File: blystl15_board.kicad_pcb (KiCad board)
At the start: 2 copper layers, 3 parts, among them P2 ARM JTAG/SWD

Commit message: Schematic Draft
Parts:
- removed BT1: BAT-HLD-003-SMT, 1_I-SYST_inc:BAT_BAT-HLD-003-SMT
- removed P2: ARM JTAG/SWD, 1_I-SYST_inc:CON10_2X5_DUK_FTSH_SAI-M
- added C1: 4.7 μF, Capacitor_SMD:C_0603_1608Metric, F.Cu at (151.9, 106.8)
- added C2: 10000 pF, Capacitor_SMD:C_0402_1005Metric, F.Cu at (162.9, 90.6)
- added C3: 10µF, Capacitor_SMD:C_0603_1608Metric, F.Cu at (151.9, 109.3)
- added C4: 10000 pF, Capacitor_SMD:C_0402_1005Metric, F.Cu at (162.9, 92.6)
- added C5: 10000 pF, Capacitor_SMD:C_0402_1005Metric, F.Cu at (162.9, 94.6)
- added C6: 10000 pF, Capacitor_SMD:C_0402_1005Metric, F.Cu at (162.9, 96.6)
- added L1: 1.0µH, Inductor_SMD:L_0805_2012Metric, F.Cu at (156.2, 106.9)
- added R1: 4.7k, Resistor_SMD:R_0402_1005Metric, F.Cu at (155.4, 109.3)
- added R2: 4.7K, Resistor_SMD:R_0402_1005Metric, F.Cu at (155.4, 111.3)
- added SW2: SW_Push, Button_Switch_SMD:SW_Push_1P1T_NO_CK_KSC7xxJ, F.Cu at (144.8, 93.5)
- added SW3: SW_Push, Button_Switch_SMD:SW_Push_1P1T_NO_CK_KSC7xxJ, F.Cu at (144.8, 101.3)
- added SW4: SW_Push, Button_Switch_SMD:SW_Push_1P1T_NO_CK_KSC7xxJ, F.Cu at (144.8, 109.0)
- added U1: NPM1304-QEAA-R7, 1_I-SYST_inc:QFN50P500X500X90-33N, F.Cu at (153.9, 101.9)
- added U2: MAX30102EFD+T, 1_I-SYST_inc:21-1048_F143A5&plus_1_MXM-L, F.Cu at (160.6, 101.8)
- added U3: MAX30208CLB+T, 1_I-SYST_inc:21-100265_MXM, F.Cu at (160.4, 107.4)
- moved M1 14.8 mm to (156.7, 94.0)

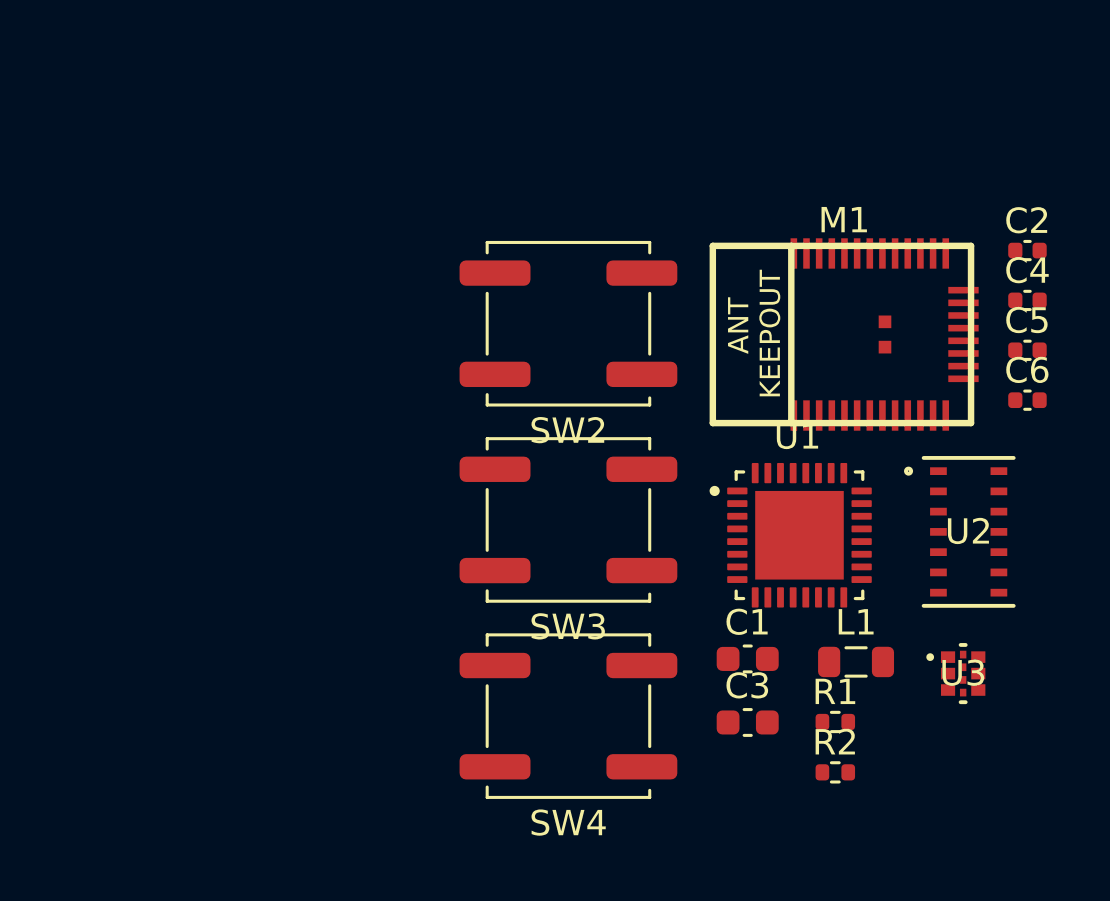
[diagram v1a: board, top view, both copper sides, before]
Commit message: All footprints imported in PCB editor
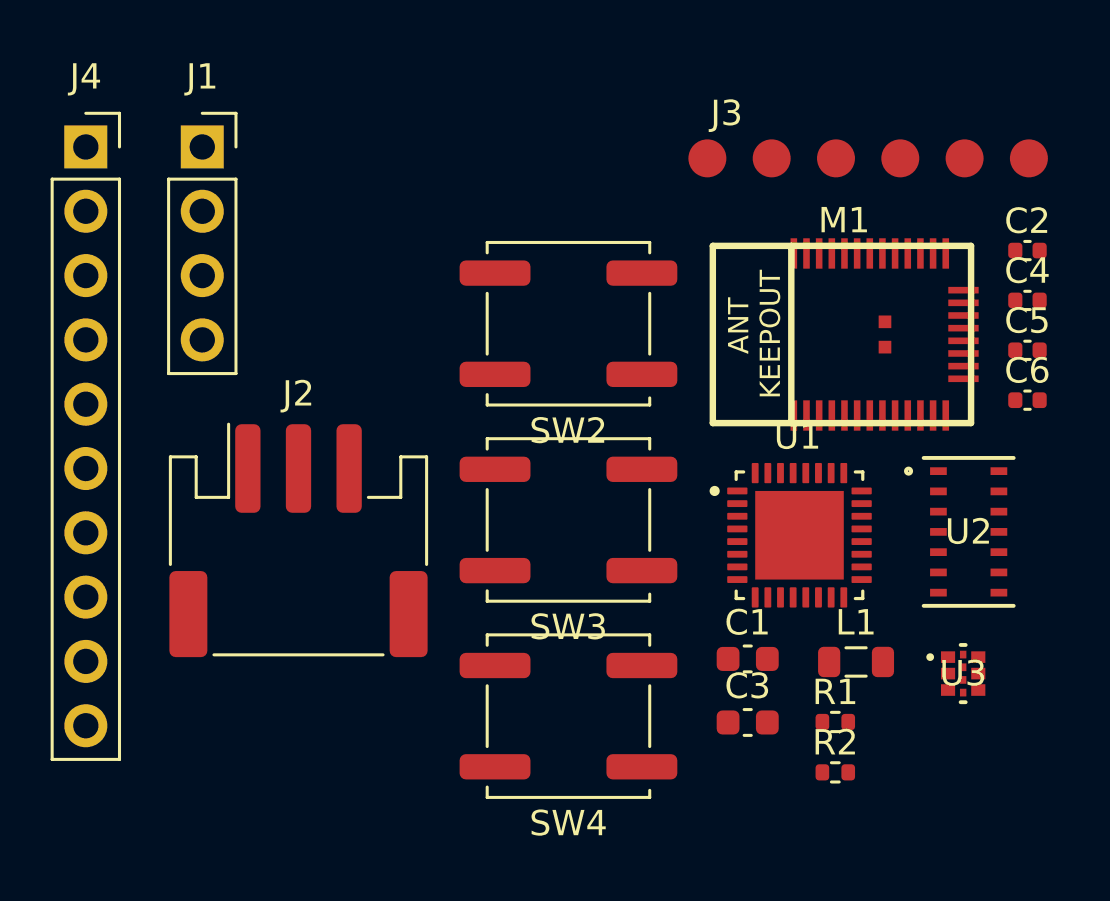
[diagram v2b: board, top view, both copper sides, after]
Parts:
- added J1: SSD1306, Connector_PinSocket_2.54mm:PinSocket_1x04_P2.54mm_Vertical, F.Cu at (130.3, 86.5)
- added J2: Conn_01x03, Connector_JST:JST_PH_S3B-PH-SM4-TB_1x03-1MP_P2.00mm_Horizontal, F.Cu at (134.2, 102.1)
- added J3: DOCK_PADS, 1_I-SYST_inc:Dock_Pads_6Pin, F.Cu at (156.7, 87.0)
- added J4: BNO085, Connector_PinSocket_2.54mm:PinSocket_1x10_P2.54mm_Vertical, F.Cu at (125.8, 86.5)

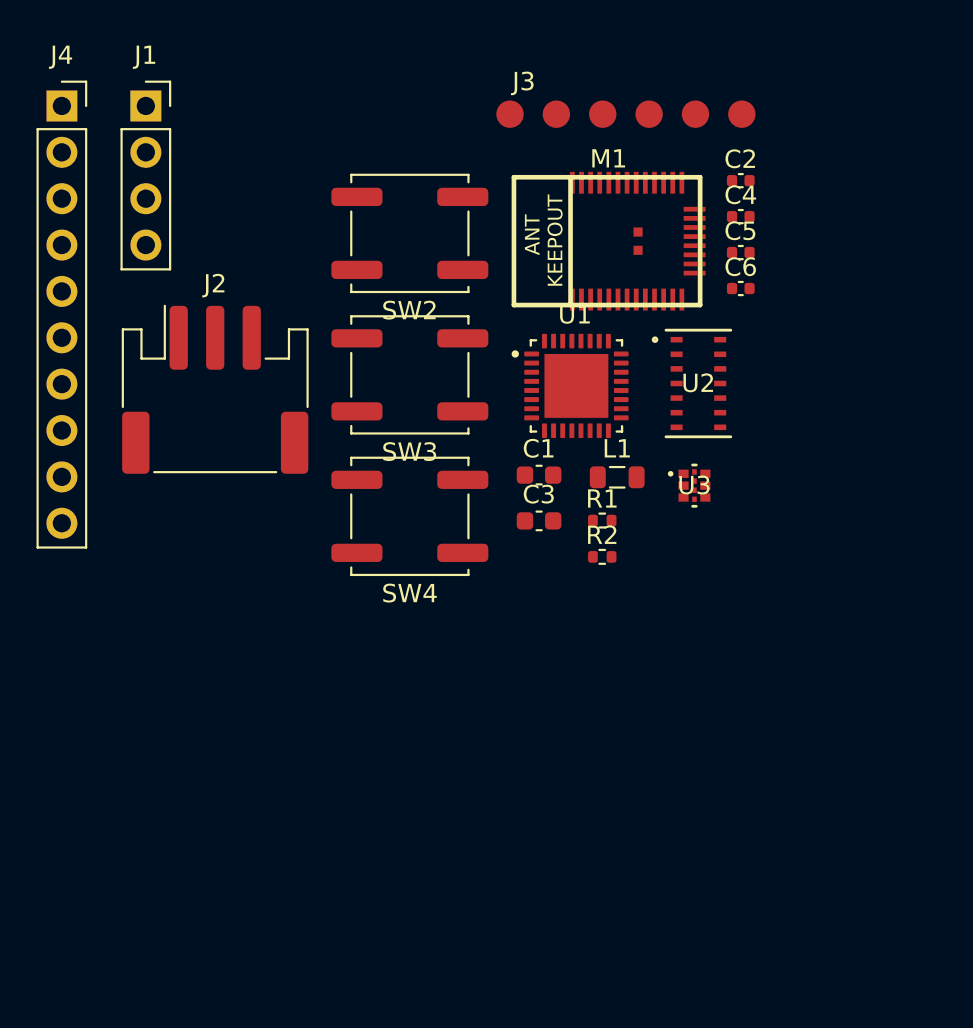
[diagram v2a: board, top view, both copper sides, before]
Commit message: Created custom footprints to match dimension of external boards
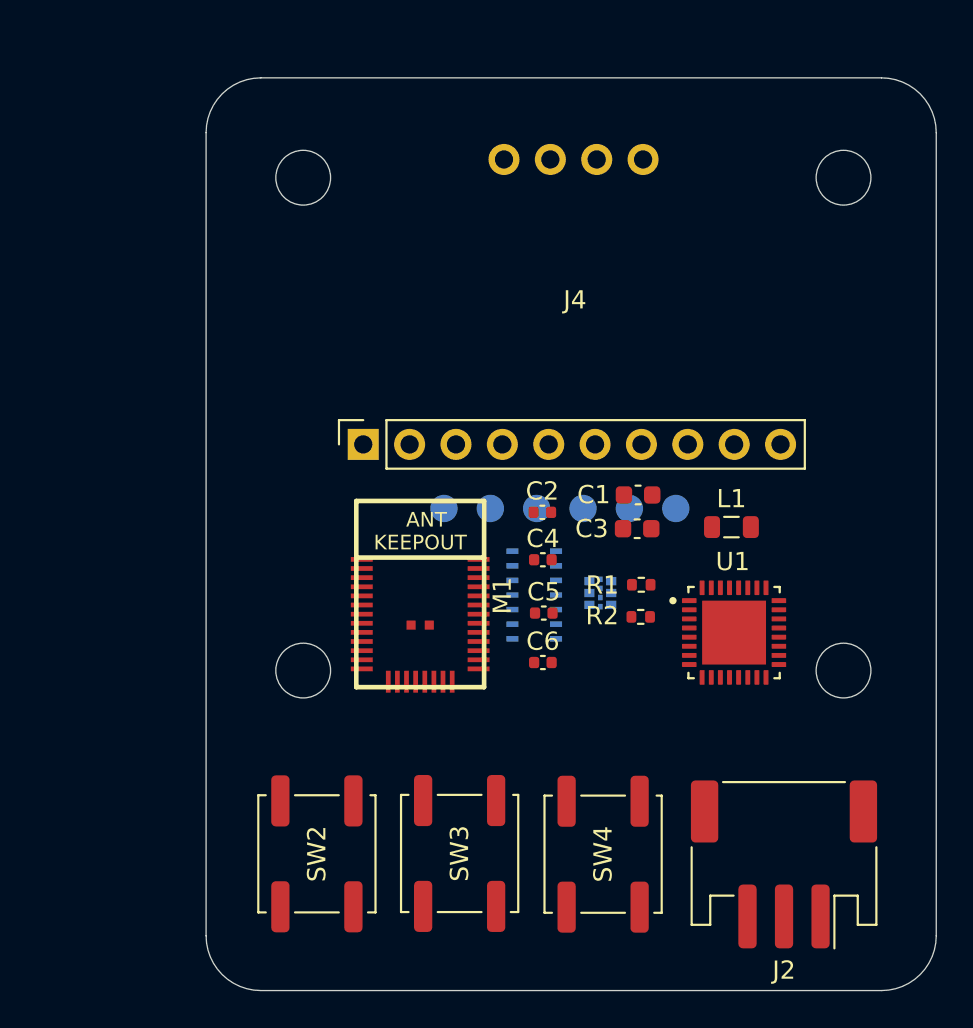
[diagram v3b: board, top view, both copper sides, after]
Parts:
- J1: footprint Connector_PinSocket_2.54mm:PinSocket_1x04_P2.54mm_Vertical -> 1_I-SYST_inc:OLED_1.3in_I2C
- J3, U2, U3: moved to B.Cu
- J4: footprint Connector_PinSocket_2.54mm:PinSocket_1x10_P2.54mm_Vertical -> 1_I-SYST_inc:BNO085_Module
- moved J2 40.6 mm to (165.3, 128.1), turned to 180 degrees
- moved SW2 34.4 mm to (139.7, 127.5), turned to 90 degrees
- moved J4 30.5 mm to (153.8, 98.5), turned to 90 degrees
- moved J1 29.2 mm to (153.8, 104.0)
- moved SW3 26.4 mm to (147.5, 127.5), turned to 90 degrees
- moved M1 23.4 mm to (145.4, 114.4), turned to -90 degrees
- moved C6 23.2 mm to (152.1, 117.0)
- moved C5 22.5 mm to (152.2, 114.3)
- moved J3 21.9 mm to (153.0, 108.6), turned to 180 degrees
- moved C4 21.7 mm to (152.1, 111.4)
- moved SW4 21.3 mm to (155.4, 127.5), turned to 90 degrees
- moved C2 21.2 mm to (152.1, 108.8)
- moved U1 16.0 mm to (162.6, 115.4)
- moved U2 14.7 mm to (151.6, 113.3), turned to 180 degrees
- moved U3 7.82 mm to (155.2, 113.2), turned to 180 degrees
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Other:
- board outline added: 40 x 50 mm

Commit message: Organized components in pcb layout editor
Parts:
- removed C2: 10000 pF, Capacitor_SMD:C_0402_1005Metric
- removed J2: Conn_01x03, Connector_JST:JST_PH_S3B-PH-SM4-TB_1x03-1MP_P2.00mm_Horizontal
- removed J3: DOCK_PADS, 1_I-SYST_inc:Dock_Pads_6Pin
- removed J4: BNO085, 1_I-SYST_inc:BNO085_Module
- removed R1: 4.7k, Resistor_SMD:R_0402_1005Metric
- removed R2: 4.7K, Resistor_SMD:R_0402_1005Metric
- added C10: 10µF, Capacitor_SMD:C_0603_1608Metric, F.Cu at (152.5, 97.0)
- added C11: 0.1µF, Capacitor_SMD:C_0603_1608Metric, F.Cu at (146.5, 99.5)
- added C12: 0.1 μF, Capacitor_SMD:C_0402_1005Metric, F.Cu at (159.0, 104.5)
- added C13: 1µF, Capacitor_SMD:C_0603_1608Metric, F.Cu at (152.0, 93.3)
- added C14: 0.1 μF, Capacitor_SMD:C_0402_1005Metric, F.Cu at (161.0, 116.0)
- added C7: 0.1 μF, Capacitor_SMD:C_0402_1005Metric, F.Cu at (159.0, 99.0)
- added C8: 0.1 μF, Capacitor_SMD:C_0402_1005Metric, F.Cu at (157.0, 95.5)
- added C9: 0.01 μF, Capacitor_SMD:C_0402_1005Metric, F.Cu at (135.0, 107.5)
- added J5: Conn_01x03, Connector_JST:JST_PH_S3B-PH-SM4-TB_1x03-1MP_P2.00mm_Horizontal, F.Cu at (147.5, 115.7)
- added J6: DOCK_PADS, 1_I_Syst.inc:Dock_Pads_6Pin, B.Cu at (152.5, 100.8)
- added R3: 10kΩ, Resistor_SMD:R_0402_1005Metric, F.Cu at (160.5, 92.5)
- added R4: 4.7kΩ, Resistor_SMD:R_0402_1005Metric, F.Cu at (163.5, 97.0)
- added R5: 4.7kΩ, Resistor_SMD:R_0402_1005Metric, F.Cu at (163.5, 93.5)
- added R6: 10kΩ, Resistor_SMD:R_0402_1005Metric, F.Cu at (158.0, 115.5)
- added U6: W25Q80DVSSIG, 1_I_Syst.inc:WIN_SS-8_WIN-L, F.Cu at (160.1, 109.6)
- added U7: OPT3001DNPRQ1, 1_I_Syst.inc:SON65P200X200X65-7N, F.Cu at (161.0, 119.0)
- added U8: LSM6DSV80X, 1_I_Syst.inc:QFN_LSM6DSV80XTR_STM-M, F.Cu at (160.0, 95.8)
- C4, C5, C6: value 10000 pF -> 0.01 μF
- J1: footprint 1_I-SYST_inc:OLED_1.3in_I2C -> 1_I_Syst.inc:OLED_1.3in_I2C
- M1: value ~ -> BLYSTL15; footprint 1_I-SYST_inc:BLYSTL15 -> 1_I_Syst.inc:BLYSTL15
- SW2, SW3, SW4: footprint Button_Switch_SMD:SW_Push_1P1T_NO_CK_KSC7xxJ -> Button_Switch_SMD:SW_Push_1P1T-MP_NO_Horizontal_Alps_SKRTLAE010
- U1: value NPM1304-QEAA-R7 -> NPM1304; footprint 1_I-SYST_inc:QFN50P500X500X90-33N -> 1_I_Syst.inc:QFN50P500X500X90-33N
- U2: footprint 1_I-SYST_inc:21-1048_F143A5&plus_1_MXM-L -> 1_I_Syst.inc:21-1048_F143A5&plus_1_MXM-L
- U3: footprint 1_I-SYST_inc:21-100265_MXM -> 1_I_Syst.inc:21-100265_MXM
- moved SW2 39.8 mm to (169.5, 101.2)
- moved SW3 39.5 mm to (169.5, 94.7)
- moved C6 26.7 mm to (166.5, 94.5), turned to 90 degrees
- moved L1 25.3 mm to (143.0, 93.4), turned to -90 degrees
- moved U1 25.0 mm to (147.8, 95.2)
- moved SW4 24.2 mm to (169.4, 107.9)
- moved C3 21.8 mm to (146.0, 91.0)
- moved C4 17.8 mm to (166.5, 101.0), turned to 90 degrees
- moved C1 17.0 mm to (143.0, 98.8), turned to 90 degrees
- moved M1 15.5 mm to (137.0, 101.3), turned to 0 degrees
- moved C5 15.0 mm to (166.0, 108.5), turned to 90 degrees
- moved U2 12.4 mm to (148.2, 101.4)
- moved U3 11.6 mm to (156.9, 101.8)
- moved J1 3.37 mm to (152.2, 101.0)
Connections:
- C6 pad 1: /P0.09 -> /P2.00
- SW3 pad 1: /P0.09 -> /P2.00
- U1 pad 18: /NTC -> /Power Management/NTC
- U1 pad 19: /VBAT -> /Power Management/VBAT
- U1 pad 21: /VBUS -> /Power Management/VBUS
- U2 pad 10: /VBAT -> /Sensors/VBAT
- U2 pad 9: /VBAT -> /Sensors/VBAT
- U3 pad 7: /P2.06 -> /P2.03
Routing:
- net /P1.09: track 0.00 -> 38.6 mm, vias 0 -> 2
- net /P1.10: track 0.00 -> 34.4 mm, vias 0 -> 1
- net /Power Management/NTC: track 0.00 -> 25.1 mm
- net Net-(U1-PVDD): track 0.00 -> 24.9 mm, vias 0 -> 2
- net /Power Management/VBAT: track 0.00 -> 24.4 mm
- net GND: track 0.00 -> 19.7 mm, vias 0 -> 10
- net /P2.07: track 0.00 -> 16.8 mm, vias 0 -> 2
- net /P0.03: track 0.00 -> 13.6 mm
- net VDD: track 0.00 -> 10.8 mm, vias 0 -> 1
- net /nRESET: track 0.00 -> 3.01 mm
- net /Power Management/VBUS: track 0.00 -> 2.45 mm
- net Net-(U1-SW1): track 0.00 -> 2.29 mm
- added copper zone on F.Cu, net /Sensors/QVAR_SWIPE
- added copper zone on In1.Cu, net GND
- added copper zone on In2.Cu, net VDD
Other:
- board size 40 x 50 mm -> 42 x 42 mm
- copper layers 2 -> 4

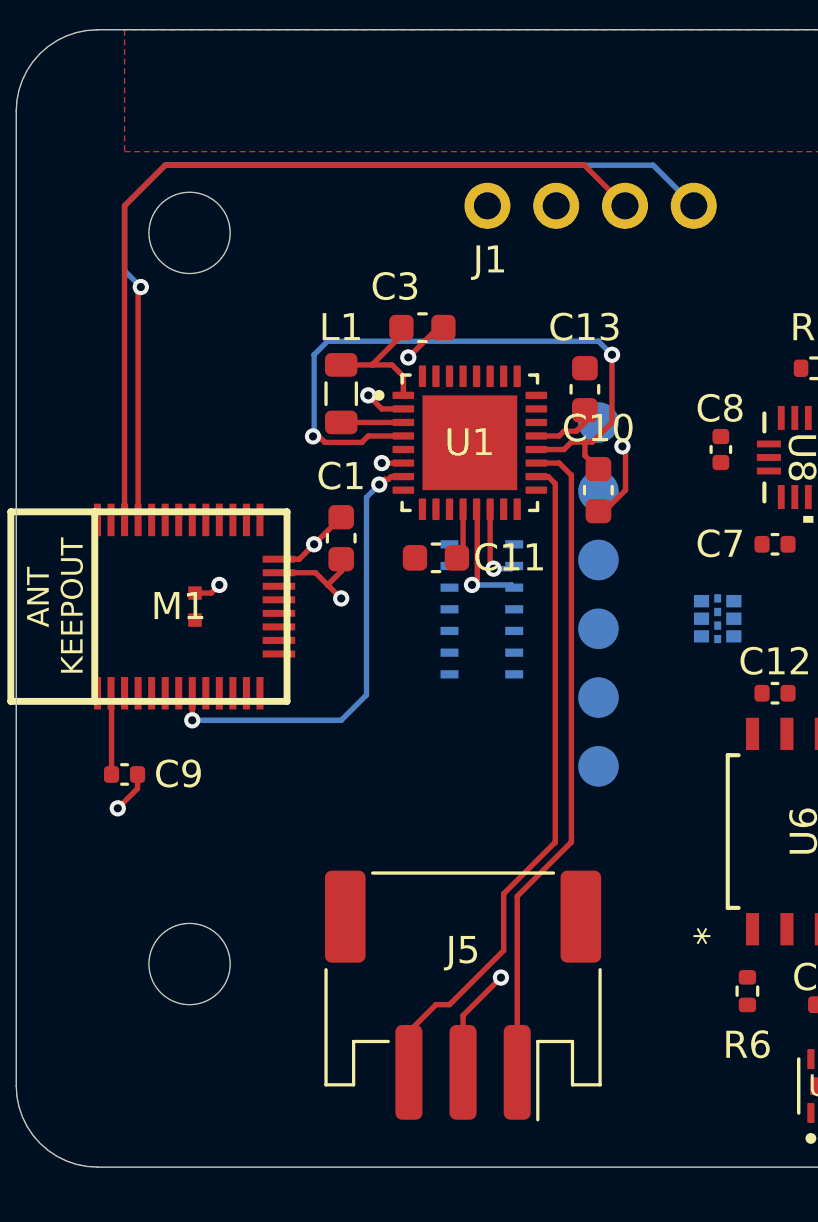
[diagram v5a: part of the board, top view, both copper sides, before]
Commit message: PCB traces started
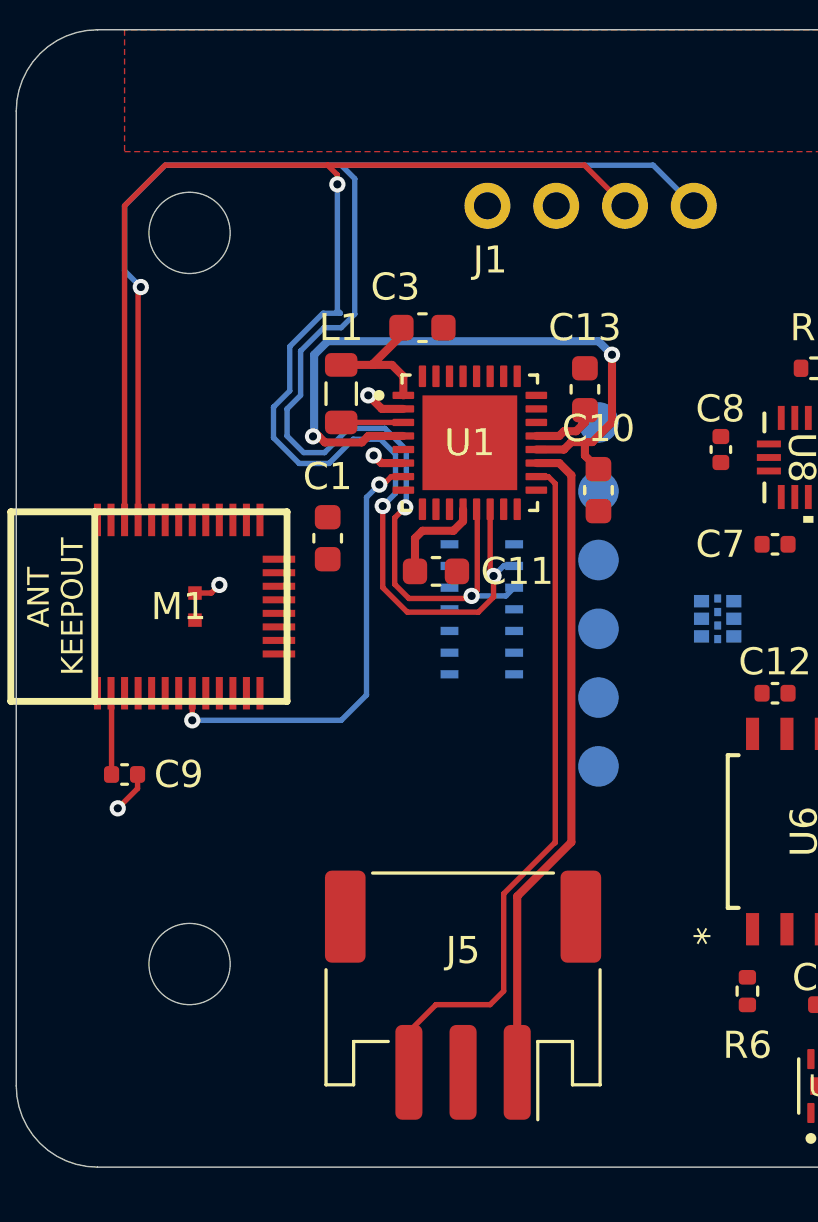
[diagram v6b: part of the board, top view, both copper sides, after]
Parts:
- moved C1 0.50 mm to (142.5, 98.8)
- moved C11 0.50 mm to (146.5, 100.0), turned to 0 degrees
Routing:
- net /P1.10: track 34.4 -> 62.5 mm, vias 1 -> 3
- net /P1.09: track 38.6 -> 64.4 mm, vias 2 -> 3
- net GND: track 19.7 -> 8.52 mm, vias 10 -> 6
- net VDD: track 10.8 -> 8.69 mm, vias 1 -> 0
- net /Power Management/NTC: track 25.1 -> 26.0 mm
- removed copper zone on In1.Cu, net GND
- removed copper zone on In2.Cu, net VDD
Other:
- copper layers 4 -> 2
